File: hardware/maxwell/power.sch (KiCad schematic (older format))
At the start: 38 parts, among them J7 Dynamo Input, J8 USB Input, J9 Battery, Q2 Q_NMOS_GDS, Q3 NDS8434, Q4 Q_NMOS_GSD, U10 LT1529, U8 TLP188, U9 Buck Regulator

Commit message: Fixed just...an unbelievable number of bugs.
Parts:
- removed Q3: NDS8434, coddingtonbear/coddingtonbear.pretty:NDS8434, symbol NDS8434
- removed Q4: Q_NMOS_GSD, adamgreig/agg-kicad/agg.pretty:SOT-23, symbol Q_NMOS_GSD
- added Q3: Q_PMOS_GDS, coddingtonbear/coddingtonbear.pretty:NDS8434, symbol Q_PMOS_GDS
- D2, D3: value 25 -> 18; footprint coddingtonbear/coddingtonbear.pretty:DIODE-VERTICAL -> adamgreig/agg-kicad/agg.pretty:DO-214AA-SMB
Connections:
- net +BATT: now also J9.1 (Pin_1), U*1.3 (VBAT)
- net GND: now also R19.2, U10.3 (GND); no longer R36.1
- net +Dynamo: now reaches C17.1, C18.2, D5.1 (K), R30.2, U*1.4 (VDD)
- net +Dynamo: now also Q3.2 (D); no longer U9.3 (OUT+)
- net BATT_CHARGE_ENABLE renamed ~BATT_CHARGE_ENABLE
- net ~BATT_CHARGE_ENABLE: now also Q3.1 (G)
- new net: Q3.3 (S), R36.1, U9.3 (OUT+)
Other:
- moved on the sheet: R19, R36
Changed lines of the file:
@@
 P 2400 1050
 F 0 "D2" V 2354 1129 50  0000 L CNN
-F 1 "25" V 2445 1129 50  0000 L CNN
-F 2 "coddingtonbear/coddingtonbear.pretty:DIODE-VERTICAL" H 2400 1050 50  0001 C CNN
+F 1 "18" V 2445 1129 50  0000 L CNN
+F 2 "adamgreig/agg-kicad/agg.pretty:DO-214AA-SMB" H 2400 1050 50  0001 C CNN
 F 3 "" H 2400 1050 50  0001 C CNN
 	1    2400 1050
@@
 P 2400 1400
 F 0 "D3" V 2446 1321 50  0000 R CNN
-F 1 "25" V 2355 1321 50  0000 R CNN
-F 2 "coddingtonbear/coddingtonbear.pretty:DIODE-VERTICAL" H 2400 1400 50  0001 C CNN
+F 1 "18" V 2355 1321 50  0000 R CNN
+F 2 "adamgreig/agg-kicad/agg.pretty:DO-214AA-SMB" H 2400 1400 50  0001 C CNN
 F 3 "" H 2400 1400 50  0001 C CNN
 	1    2400 1400
@@
 L GND #PWR041
 U 1 1 5A21058A
-P 7300 2400
-F 0 "#PWR041" H 7300 2150 50  0001 C CNN
-F 1 "GND" H 7305 2227 50  0000 C CNN
-F 2 "" H 7300 2400 50  0001 C CNN
-F 3 "" H 7300 2400 50  0001 C CNN
-	1    7300 2400
+P 7350 1900
+F 0 "#PWR041" H 7350 1650 50  0001 C CNN
+F 1 "GND" H 7355 1727 50  0000 C CNN
+F 2 "" H 7350 1900 50  0001 C CNN
+F 3 "" H 7350 1900 50  0001 C CNN
+	1    7350 1900
 	1    0    0    -1
 $EndComp
@@
 L R R19
 U 1 1 5A210718
-P 8000 1650
-F 0 "R19" H 8070 1696 50  0000 L CNN
-F 1 "2k" H 8070 1605 50  0000 L CNN
-F 2 "coddingtonbear/coddingtonbear.pretty:0805_Milling" V 7930 1650 50  0001 C CNN
-F 3 "" H 8000 1650 50  0001 C CNN
-	1    8000 1650
+P 7450 1650
+F 0 "R19" H 7520 1696 50  0000 L CNN
+F 1 "2k" H 7520 1605 50  0000 L CNN
+F 2 "coddingtonbear/coddingtonbear.pretty:0805_Milling" V 7380 1650 50  0001 C CNN
+F 3 "" H 7450 1650 50  0001 C CNN
+	1    7450 1650
 	1    0    0    -1
 $EndComp
 Text GLabel 6400 2200 2    60   Output ~ 0
 ~BATT_CHARGING
-$Comp
-L +BATT #PWR043
-U 1 1 5A210C7A
-P 8400 850
-F 0 "#PWR043" H 8400 700 50  0001 C CNN
-F 1 "+BATT" H 8415 1023 50  0000 C CNN
-F 2 "" H 8400 850 50  0001 C CNN
-F 3 "" H 8400 850 50  0001 C CNN
-	1    8400 850
-	1    0    0    -1
-$EndComp
 Text Notes 4400 1550 0    60   ~ 0
 Tune to 4V
@@
 Text GLabel 2450 3900 0    60   Input ~ 0
 ENABLE_BATT_POWER
-$Comp
-L NDS8434 Q3
-U 1 1 5A25C576
-P 8300 1050
-F 0 "Q3" H 8491 1004 50  0000 L CNN
-F 1 "NDS8434" H 8491 1095 50  0000 L CNN
-F 2 "coddingtonbear/coddingtonbear.pretty:NDS8434" H 8500 950 50  0001 L CIN
-F 3 "" H 8300 1050 50  0000 L CNN
-	1    8300 1050
-	1    0    0    1
-$EndComp
-$Comp
-L GND #PWR051
-U 1 1 5A25CAAF
-P 8100 1000
-F 0 "#PWR051" H 8100 750 50  0001 C CNN
-F 1 "GND" H 8105 827 50  0000 C CNN
-F 2 "" H 8100 1000 50  0001 C CNN
-F 3 "" H 8100 1000 50  0001 C CNN
-	1    8100 1000
-	1    0    0    -1
-$EndComp
 Text GLabel 1300 1200 0    60   Input ~ 0
 AC_NEUTRAL
@@
 	-1   0    0    1
 $EndComp
-Text GLabel 8050 2100 2    60   Input ~ 0
-BATT_CHARGE_ENABLE
+Text GLabel 5500 950  2    60   Input ~ 0
+~BATT_CHARGE_ENABLE
 $Comp
 L R R34
@@
 Text GLabel 4400 650  2    60   Output ~ 0
 DYNAMO_VOLTAGE
+$Comp
+L R R36
+U 1 1 5A27BDA2
+P 5350 750
+F 0 "R36" H 5420 796 50  0000 L CNN
+F 1 "10k" H 5420 705 50  0000 L CNN
+F 2 "coddingtonbear/coddingtonbear.pretty:0805_Milling" V 5280 750 50  0001 C CNN
+F 3 "" H 5350 750 50  0001 C CNN
+	1    5350 750
+	1    0    0    -1
+$EndComp
+$Comp
+L +BATT #PWR043
+U 1 1 5A210C7A
+P 8250 1200
+F 0 "#PWR043" H 8250 1050 50  0001 C CNN
+F 1 "+BATT" H 8265 1373 50  0000 C CNN
+F 2 "" H 8250 1200 50  0001 C CNN
+F 3 "" H 8250 1200 50  0001 C CNN
+	1    8250 1200
+	1    0    0    -1
+$EndComp
 Wire Wire Line
 	2400 1250 2400 1200
@@
 	7850 3400 7500 3400
 Wire Wire Line
-	7500 3400 7500 3500
+	7500 3500 7500 3400
 Connection ~ 7100 3500
 Wire Wire Line
@@
 Wire Wire Line
 	3700 2350 3950 2350
-Connection ~ 5400 1250
-Wire Wire Line
-	4200 1250 3650 1250
+Wire Wire Line
+	3650 1250 4200 1250
 Wire Wire Line
 	7400 3100 8600 3100
@@
 	7500 3200 7500 3100
 Wire Wire Line
-	5150 1250 6400 1250
-Wire Wire Line
-	5400 2350 5400 1250
-Wire Wire Line
-	7500 3500 5450 3500
+	5600 1250 6400 1250
+Wire Wire Line
+	5450 3500 7500 3500
 Wire Wire Line
 	5900 1300 5900 1250
@@
 	5950 3200 6200 3200
 Wire Wire Line
-	4250 2350 6650 2350
-Wire Wire Line
 	6650 2650 6650 4150
-Connection ~ 5400 2350
 Wire Wire Line
 	6650 4150 6350 4150
@@
 	1500 3500 1350 3500
 Wire Wire Line
-	7300 1750 7300 2400
-Wire Wire Line
 	4000 850  3800 850
 Wire Wire Line
@@
 	4300 650  4400 650
 Wire Wire Line
-	7300 1500 8000 1500
-Connection ~ 7300 1800
-Wire Wire Line
-	7600 1800 7300 1800
-$Comp
-L Q_NMOS_GSD Q4
-U 1 1 5A277444
-P 7800 1900
-F 0 "Q4" V 8143 1900 50  0000 C CNN
-F 1 "Q_NMOS_GSD" V 8052 1900 50  0000 C CNN
-F 2 "adamgreig/agg-kicad/agg.pretty:SOT-23" H 8000 2000 50  0001 C CNN
-F 3 "" H 7800 1900 50  0001 C CNN
-	1    7800 1900
-	0    1    -1   0
-$EndComp
-$Comp
-L R R36
-U 1 1 5A27BDA2
-P 7550 2400
-F 0 "R36" H 7620 2446 50  0000 L CNN
-F 1 "10k" H 7620 2355 50  0000 L CNN
-F 2 "coddingtonbear/coddingtonbear.pretty:0805_Milling" V 7480 2400 50  0001 C CNN
-F 3 "" H 7550 2400 50  0001 C CNN
-	1    7550 2400
-	0    -1   -1   0
-$EndComp
-Wire Wire Line
-	7300 2400 7400 2400
-Wire Wire Line
-	7700 2400 7800 2400
-Wire Wire Line
-	7800 2400 7800 2100
-Wire Wire Line
-	7800 2100 8050 2100
+	5200 1250 5150 1250
+Wire Wire Line
+	5350 900  5350 950
+Wire Wire Line
+	5350 600  5200 600
+Wire Wire Line
+	5200 600  5200 1250
+Wire Wire Line
+	8250 1200 8250 1250
+Connection ~ 8250 1250
+Wire Wire Line
+	7300 1500 7450 1500
+Wire Wire Line
+	7300 1800 7450 1800
+Wire Wire Line
+	7300 1800 7300 1750
+Wire Wire Line
+	7350 1900 7350 1800
+Connection ~ 7350 1800
+Wire Wire Line
+	4250 2350 6650 2350
+Wire Wire Line
+	5600 1250 5600 2350
+Connection ~ 5600 2350
+Wire Wire Line
+	5350 950  5500 950
+Connection ~ 5400 950
+$Comp
+L Q_PMOS_GDS Q3
+U 1 1 5A2B17F5
+P 5400 1150
+F 0 "Q3" V 5650 1150 50  0000 C CNN
+F 1 "Q_PMOS_GDS" V 5741 1150 50  0000 C CNN
+F 2 "coddingtonbear/coddingtonbear.pretty:NDS8434" H 5600 1250 50  0001 C CNN
+F 3 "" H 5400 1150 50  0001 C CNN
+	1    5400 1150
+	0    1    1    0
+$EndComp
+Text Label 5950 1250 0    60   ~ 0
++Dynamo
+Connection ~ 7050 3500
 $EndSCHEMATC

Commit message: Adding CANBus termination resistors.
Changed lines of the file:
@@
 	7850 3400 7500 3400
 Wire Wire Line
-	7500 3500 7500 3400
+	7500 3400 7500 3500
 Connection ~ 7100 3500
 Wire Wire Line
@@
 	5600 1250 6400 1250
 Wire Wire Line
-	5450 3500 7500 3500
+	7500 3500 5450 3500
 Wire Wire Line
 	5900 1300 5900 1250

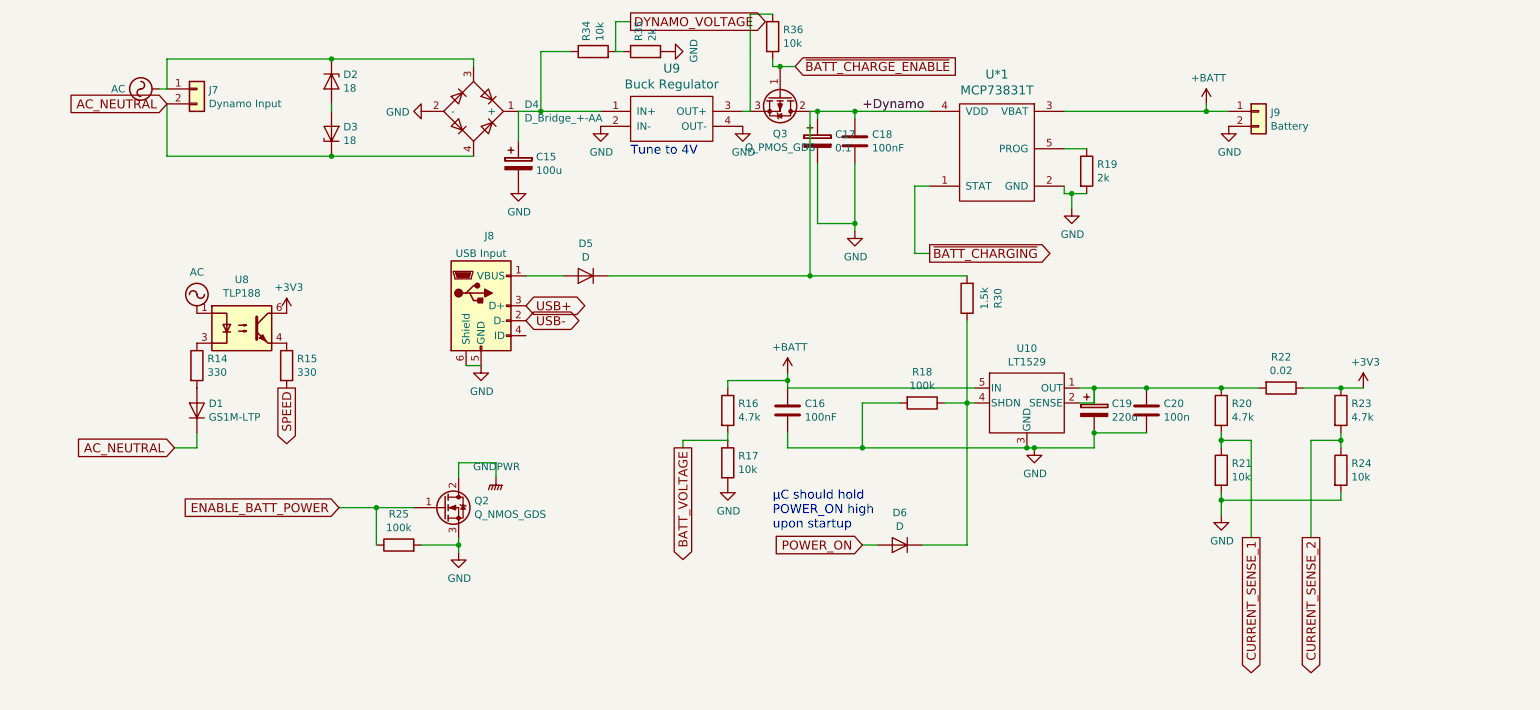
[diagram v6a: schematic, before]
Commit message: Move current measurement to battery side of ldo; obviously.  Also, remove now-redundant second current sense trace.
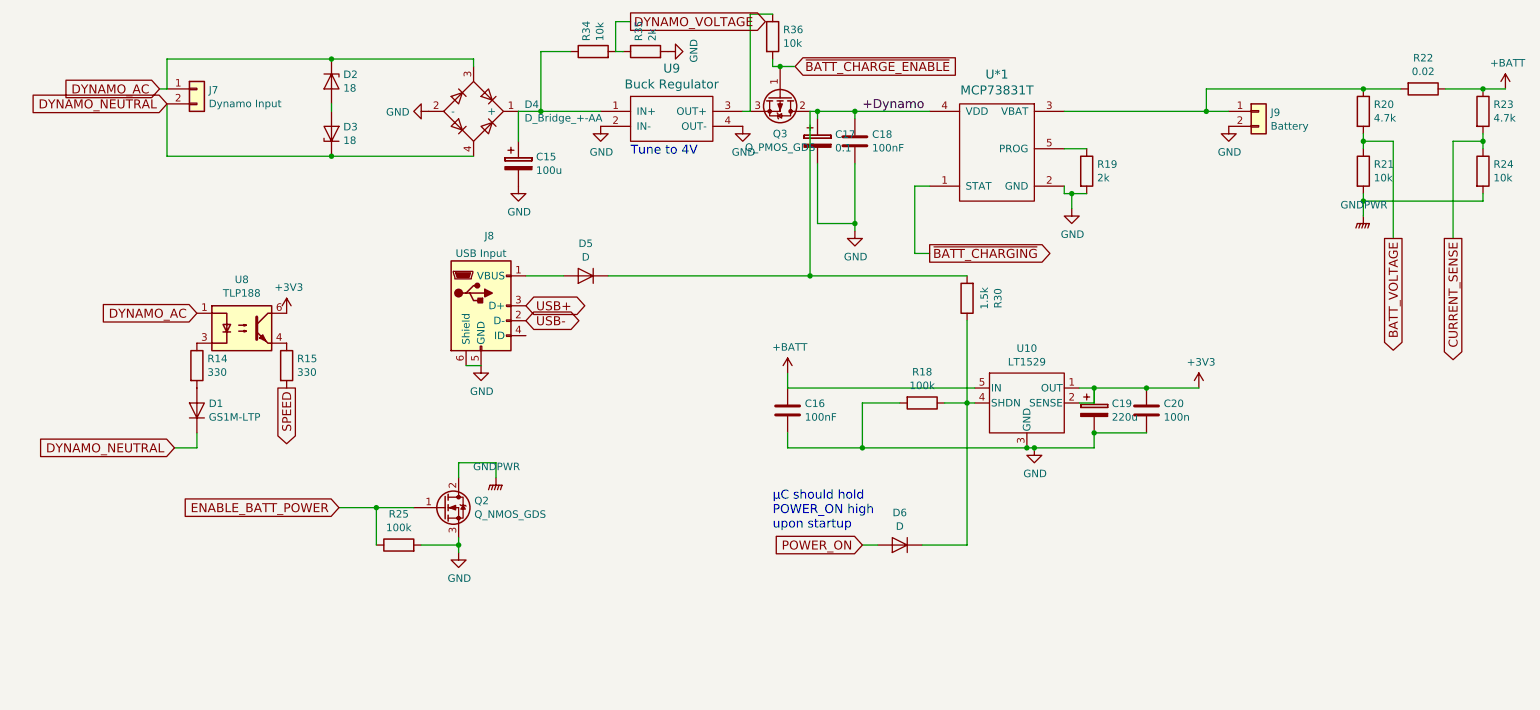
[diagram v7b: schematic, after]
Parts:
- removed R16: 4.7k, coddingtonbear/coddingtonbear.pretty:0805_Milling, symbol R
- removed R17: 10k, coddingtonbear/coddingtonbear.pretty:0805_Milling, symbol R
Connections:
- net CURRENT_SENSE_1 is gone; now on net BATT_VOLTAGE: R20.2, R21.1
- net +3V3: now also C19.1, C20.2, U10.1 (OUT), U10.2 (SENSE); no longer R22.1, R23.1
- net +BATT: now also R22.1, R23.1; no longer J9.1 (Pin_1), U*1.3 (VBAT)
- net GND: no longer R21.2, R24.2
- net GNDPWR: now also R21.2, R24.2
- net AC renamed DYNAMO_AC
- net AC_NEUTRAL renamed DYNAMO_NEUTRAL
- net CURRENT_SENSE_2 renamed CURRENT_SENSE
- new net: J9.1 (Pin_1), R20.1, R22.2, U*1.3 (VBAT)
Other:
- moved on the sheet: R20, R21, R22, R23, R24
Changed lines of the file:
@@
-$EndComp
-$Comp
-L AC #PWR030
-U 1 1 5A1FF250
-P 1250 1100
-F 0 "#PWR030" H 1250 1000 50  0001 C CNN
-F 1 "AC" V 1250 1329 50  0000 L CNN
-F 2 "" H 1250 1100 50  0001 C CNN
-F 3 "" H 1250 1100 50  0001 C CNN
-	1    1250 1100
-	0    -1   -1   0
 $EndComp
 $Comp
@@
 $EndComp
 $Comp
-L AC #PWR031
-U 1 1 5A1FF26A
-P 1500 2600
-F 0 "#PWR031" H 1500 2500 50  0001 C CNN
-F 1 "AC" H 1500 2875 50  0000 C CNN
-F 2 "" H 1500 2600 50  0001 C CNN
-F 3 "" H 1500 2600 50  0001 C CNN
-	1    1500 2600
-	1    0    0    -1
-$EndComp
-$Comp
 L R R15
 U 1 1 5A1FF270
@@
 L +3V3 #PWR035
 U 1 1 5A1FFDA9
-P 9300 3100
-F 0 "#PWR035" H 9300 2950 50  0001 C CNN
-F 1 "+3V3" H 9315 3273 50  0000 C CNN
-F 2 "" H 9300 3100 50  0001 C CNN
-F 3 "" H 9300 3100 50  0001 C CNN
-	1    9300 3100
+P 8200 3100
+F 0 "#PWR035" H 8200 2950 50  0001 C CNN
+F 1 "+3V3" H 8215 3273 50  0000 C CNN
+F 2 "" H 8200 3100 50  0001 C CNN
+F 3 "" H 8200 3100 50  0001 C CNN
+	1    8200 3100
 	1    0    0    -1
 $EndComp
@@
 L R R20
 U 1 1 5A245A23
-P 8350 3250
-F 0 "R20" H 8420 3296 50  0000 L CNN
-F 1 "4.7k" H 8420 3205 50  0000 L CNN
-F 2 "coddingtonbear/coddingtonbear.pretty:0805_Milling" V 8280 3250 50  0001 C CNN
-F 3 "" H 8350 3250 50  0001 C CNN
-	1    8350 3250
+P 9300 1250
+F 0 "R20" H 9370 1296 50  0000 L CNN
+F 1 "4.7k" H 9370 1205 50  0000 L CNN
+F 2 "coddingtonbear/coddingtonbear.pretty:0805_Milling" V 9230 1250 50  0001 C CNN
+F 3 "" H 9300 1250 50  0001 C CNN
+	1    9300 1250
 	1    0    0    -1
 $EndComp
@@
 L R R21
 U 1 1 5A245A89
-P 8350 3650
-F 0 "R21" H 8420 3696 50  0000 L CNN
-F 1 "10k" H 8420 3605 50  0000 L CNN
-F 2 "coddingtonbear/coddingtonbear.pretty:0805_Milling" V 8280 3650 50  0001 C CNN
-F 3 "" H 8350 3650 50  0001 C CNN
-	1    8350 3650
+P 9300 1650
+F 0 "R21" H 9370 1696 50  0000 L CNN
+F 1 "10k" H 9370 1605 50  0000 L CNN
+F 2 "coddingtonbear/coddingtonbear.pretty:0805_Milling" V 9230 1650 50  0001 C CNN
+F 3 "" H 9300 1650 50  0001 C CNN
+	1    9300 1650
 	1    0    0    -1
 $EndComp
@@
 L R R23
 U 1 1 5A245B4A
-P 9150 3250
-F 0 "R23" H 9220 3296 50  0000 L CNN
-F 1 "4.7k" H 9220 3205 50  0000 L CNN
-F 2 "coddingtonbear/coddingtonbear.pretty:0805_Milling" V 9080 3250 50  0001 C CNN
-F 3 "" H 9150 3250 50  0001 C CNN
-	1    9150 3250
+P 10100 1250
+F 0 "R23" H 10170 1296 50  0000 L CNN
+F 1 "4.7k" H 10170 1205 50  0000 L CNN
+F 2 "coddingtonbear/coddingtonbear.pretty:0805_Milling" V 10030 1250 50  0001 C CNN
+F 3 "" H 10100 1250 50  0001 C CNN
+	1    10100 1250
 	1    0    0    -1
 $EndComp
@@
 L R R24
 U 1 1 5A245B93
-P 9150 3650
-F 0 "R24" H 9220 3696 50  0000 L CNN
-F 1 "10k" H 9220 3605 50  0000 L CNN
-F 2 "coddingtonbear/coddingtonbear.pretty:0805_Milling" V 9080 3650 50  0001 C CNN
-F 3 "" H 9150 3650 50  0001 C CNN
-	1    9150 3650
+P 10100 1650
+F 0 "R24" H 10170 1696 50  0000 L CNN
+F 1 "10k" H 10170 1605 50  0000 L CNN
+F 2 "coddingtonbear/coddingtonbear.pretty:0805_Milling" V 10030 1650 50  0001 C CNN
+F 3 "" H 10100 1650 50  0001 C CNN
+	1    10100 1650
 	1    0    0    -1
 $EndComp
@@
 L R R22
 U 1 1 5A246038
-P 8750 3100
-F 0 "R22" V 8543 3100 50  0000 C CNN
-F 1 "0.02" V 8634 3100 50  0000 C CNN
-F 2 "coddingtonbear/coddingtonbear.pretty:0805_Milling" V 8680 3100 50  0001 C CNN
-F 3 "" H 8750 3100 50  0001 C CNN
-	1    8750 3100
+P 9700 1100
+F 0 "R22" V 9493 1100 50  0000 C CNN
+F 1 "0.02" V 9584 1100 50  0000 C CNN
+F 2 "coddingtonbear/coddingtonbear.pretty:0805_Milling" V 9630 1100 50  0001 C CNN
+F 3 "" H 9700 1100 50  0001 C CNN
+	1    9700 1100
 	0    1    1    0
 $EndComp
-$Comp
-L GND #PWR047
-U 1 1 5A24633B
-P 8350 3950
-F 0 "#PWR047" H 8350 3700 50  0001 C CNN
-F 1 "GND" H 8355 3777 50  0000 C CNN
-F 2 "" H 8350 3950 50  0001 C CNN
-F 3 "" H 8350 3950 50  0001 C CNN
-	1    8350 3950
-	1    0    0    -1
-$EndComp
-Text GLabel 8550 4100 3    60   Output ~ 0
-CURRENT_SENSE_1
-Text GLabel 8950 4100 3    60   Output ~ 0
-CURRENT_SENSE_2
-$Comp
-L R R16
-U 1 1 5A246B28
-P 5050 3250
-F 0 "R16" H 5120 3296 50  0000 L CNN
-F 1 "4.7k" H 5120 3205 50  0000 L CNN
-F 2 "coddingtonbear/coddingtonbear.pretty:0805_Milling" V 4980 3250 50  0001 C CNN
-F 3 "" H 5050 3250 50  0001 C CNN
-	1    5050 3250
-	1    0    0    -1
-$EndComp
-$Comp
-L R R17
-U 1 1 5A246B87
-P 5050 3600
-F 0 "R17" H 5120 3646 50  0000 L CNN
-F 1 "10k" H 5120 3555 50  0000 L CNN
-F 2 "coddingtonbear/coddingtonbear.pretty:0805_Milling" V 4980 3600 50  0001 C CNN
-F 3 "" H 5050 3600 50  0001 C CNN
-	1    5050 3600
-	1    0    0    -1
-$EndComp
-Text GLabel 4750 3500 3    60   Output ~ 0
+Text GLabel 9900 2100 3    60   Output ~ 0
+CURRENT_SENSE
+Text GLabel 9500 2100 3    60   Output ~ 0
 BATT_VOLTAGE
-$Comp
-L GND #PWR048
-U 1 1 5A246E28
-P 5050 3750
-F 0 "#PWR048" H 5050 3500 50  0001 C CNN
-F 1 "GND" H 5055 3577 50  0000 C CNN
-F 2 "" H 5050 3750 50  0001 C CNN
-F 3 "" H 5050 3750 50  0001 C CNN
-	1    5050 3750
-	1    0    0    -1
-$EndComp
 $Comp
 L CP C17
@@
 ENABLE_BATT_POWER
 Text GLabel 1300 1200 0    60   Input ~ 0
-AC_NEUTRAL
+DYNAMO_NEUTRAL
 Text GLabel 1350 3500 0    60   Input ~ 0
-AC_NEUTRAL
+DYNAMO_NEUTRAL
 $Comp
 L R R30
@@
 L +BATT #PWR043
 U 1 1 5A210C7A
-P 8250 1200
-F 0 "#PWR043" H 8250 1050 50  0001 C CNN
-F 1 "+BATT" H 8265 1373 50  0000 C CNN
-F 2 "" H 8250 1200 50  0001 C CNN
-F 3 "" H 8250 1200 50  0001 C CNN
-	1    8250 1200
+P 10250 1100
+F 0 "#PWR043" H 10250 950 50  0001 C CNN
+F 1 "+BATT" H 10265 1273 50  0000 C CNN
+F 2 "" H 10250 1100 50  0001 C CNN
+F 3 "" H 10250 1100 50  0001 C CNN
+	1    10250 1100
 	1    0    0    -1
 $EndComp
@@
 	3650 1250 4200 1250
 Wire Wire Line
-	7400 3100 8600 3100
+	8250 1100 9550 1100
 Wire Wire Line
 	7400 3200 7500 3200
@@
 Wire Wire Line
 	5450 3100 6700 3100
-Wire Wire Line
-	5450 3000 5450 3100
 Wire Wire Line
 	5450 3500 5450 3400
@@
 Wire Wire Line
 	6300 2200 6400 2200
-Connection ~ 8350 3100
-Wire Wire Line
-	8900 3100 9300 3100
-Wire Wire Line
-	8350 3400 8350 3500
-Wire Wire Line
-	9150 3400 9150 3500
-Connection ~ 9150 3100
-Wire Wire Line
-	8350 3800 8350 3950
-Wire Wire Line
-	8350 3850 9150 3850
-Wire Wire Line
-	9150 3850 9150 3800
-Connection ~ 8350 3850
-Wire Wire Line
-	8350 3450 8550 3450
-Wire Wire Line
-	8550 3450 8550 4100
-Connection ~ 8350 3450
-Wire Wire Line
-	8950 4100 8950 3450
-Wire Wire Line
-	8950 3450 9150 3450
-Connection ~ 9150 3450
-Wire Wire Line
-	5450 3050 5050 3050
-Wire Wire Line
-	5050 3050 5050 3100
-Connection ~ 5450 3050
-Wire Wire Line
-	5050 3400 5050 3450
-Wire Wire Line
-	5050 3450 4750 3450
-Wire Wire Line
-	4750 3450 4750 3500
+Connection ~ 9300 1100
+Wire Wire Line
+	9850 1100 10250 1100
+Wire Wire Line
+	9300 1400 9300 1500
+Wire Wire Line
+	10100 1400 10100 1500
+Connection ~ 10100 1100
+Wire Wire Line
+	9300 1800 9300 1950
+Wire Wire Line
+	9300 1850 10100 1850
+Wire Wire Line
+	10100 1850 10100 1800
+Connection ~ 9300 1850
+Wire Wire Line
+	9300 1450 9500 1450
+Wire Wire Line
+	9500 1450 9500 2100
+Connection ~ 9300 1450
+Wire Wire Line
+	9900 2100 9900 1450
+Wire Wire Line
+	9900 1450 10100 1450
+Connection ~ 10100 1450
 Wire Wire Line
 	7300 1250 8400 1250
@@
 	5200 600  5200 1250
 Wire Wire Line
-	8250 1200 8250 1250
+	8250 1100 8250 1250
 Connection ~ 8250 1250
 Wire Wire Line
@@
 +Dynamo
 Connection ~ 7050 3500
+Wire Wire Line
+	7400 3100 8200 3100
+Wire Wire Line
+	5450 3000 5450 3100
+$Comp
+L GNDPWR #PWR020
+U 1 1 5A2C7A67
+P 9300 1950
+F 0 "#PWR020" H 9300 1750 50  0001 C CNN
+F 1 "GNDPWR" H 9304 2024 50  0000 C CNN
+F 2 "" H 9300 1900 50  0001 C CNN
+F 3 "" H 9300 1900 50  0001 C CNN
+	1    9300 1950
+	1    0    0    -1
+$EndComp
+Text GLabel 1250 1100 0    60   Input ~ 0
+DYNAMO_AC
+Text GLabel 1500 2600 0    60   Input ~ 0
+DYNAMO_AC
 $EndSCHEMATC
